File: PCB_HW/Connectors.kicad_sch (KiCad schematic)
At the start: 14 parts, among them J10 Conn_01x04_MountingPin, J11 Conn_01x04_MountingPin, J12 Conn_01x06_MountingPin, J13 Conn_01x08_MountingPin, J14 Conn_01x08, J15 Conn_01x04_MountingPin, J2 Conn_01x04_MountingPin, J3 Conn_01x04_MountingPin, J4 Conn_01x04_MountingPin, J5 Conn_01x04_MountingPin, J6 Conn_01x08_MountingPin, J7 Conn_01x04_MountingPin, J8 Conn_01x06, J9 Conn_01x02_MountingPin

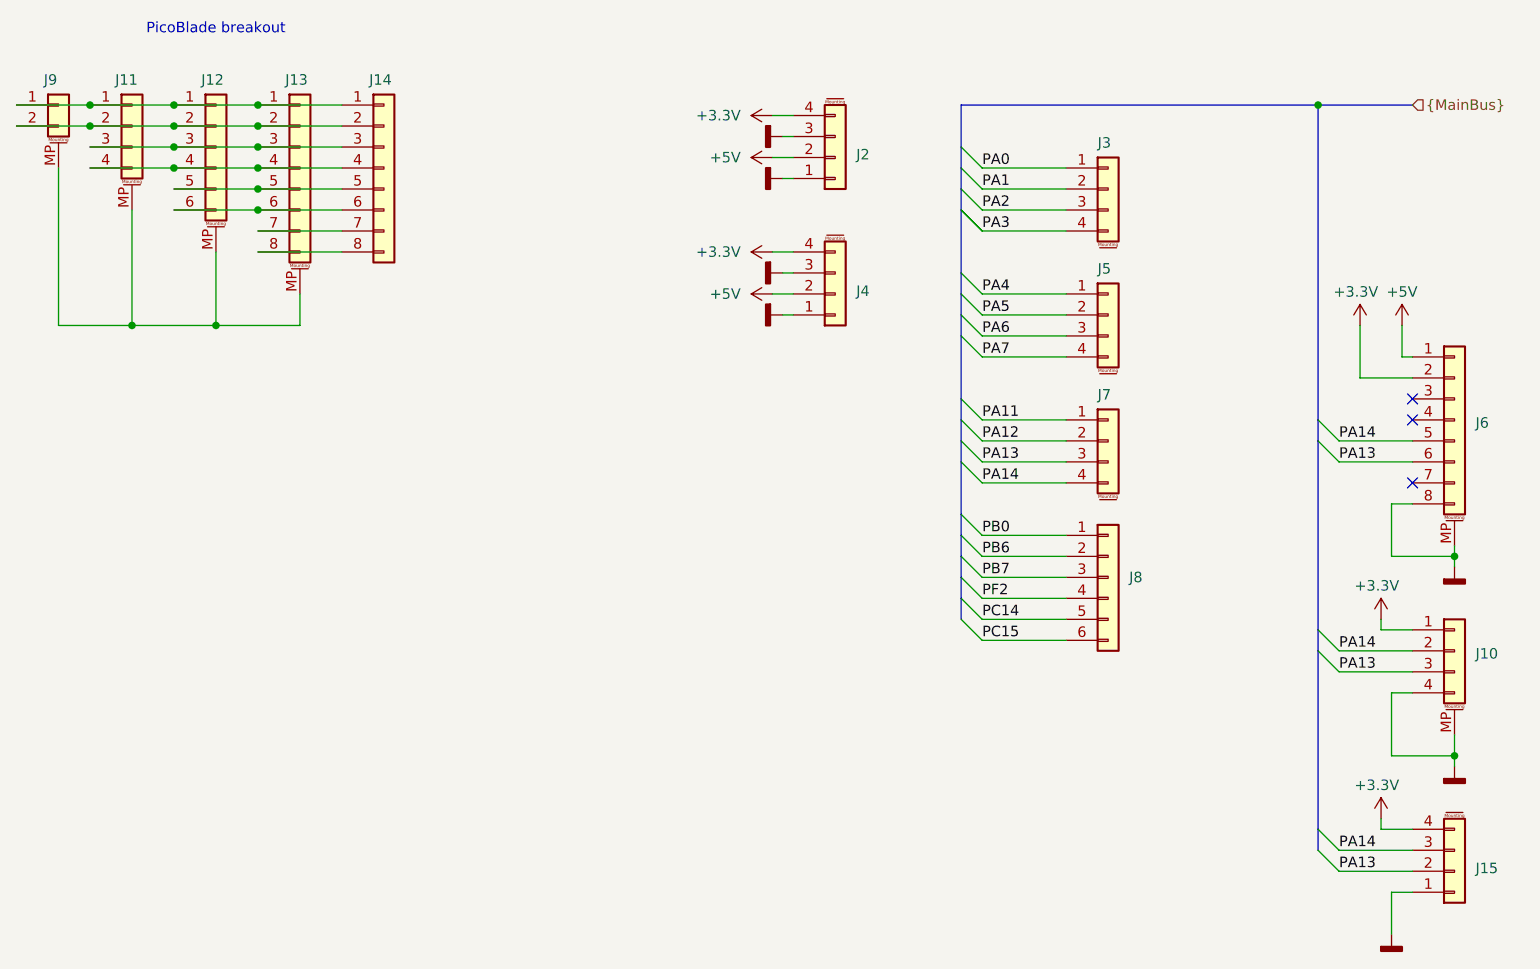
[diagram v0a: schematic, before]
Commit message: Some parts routed
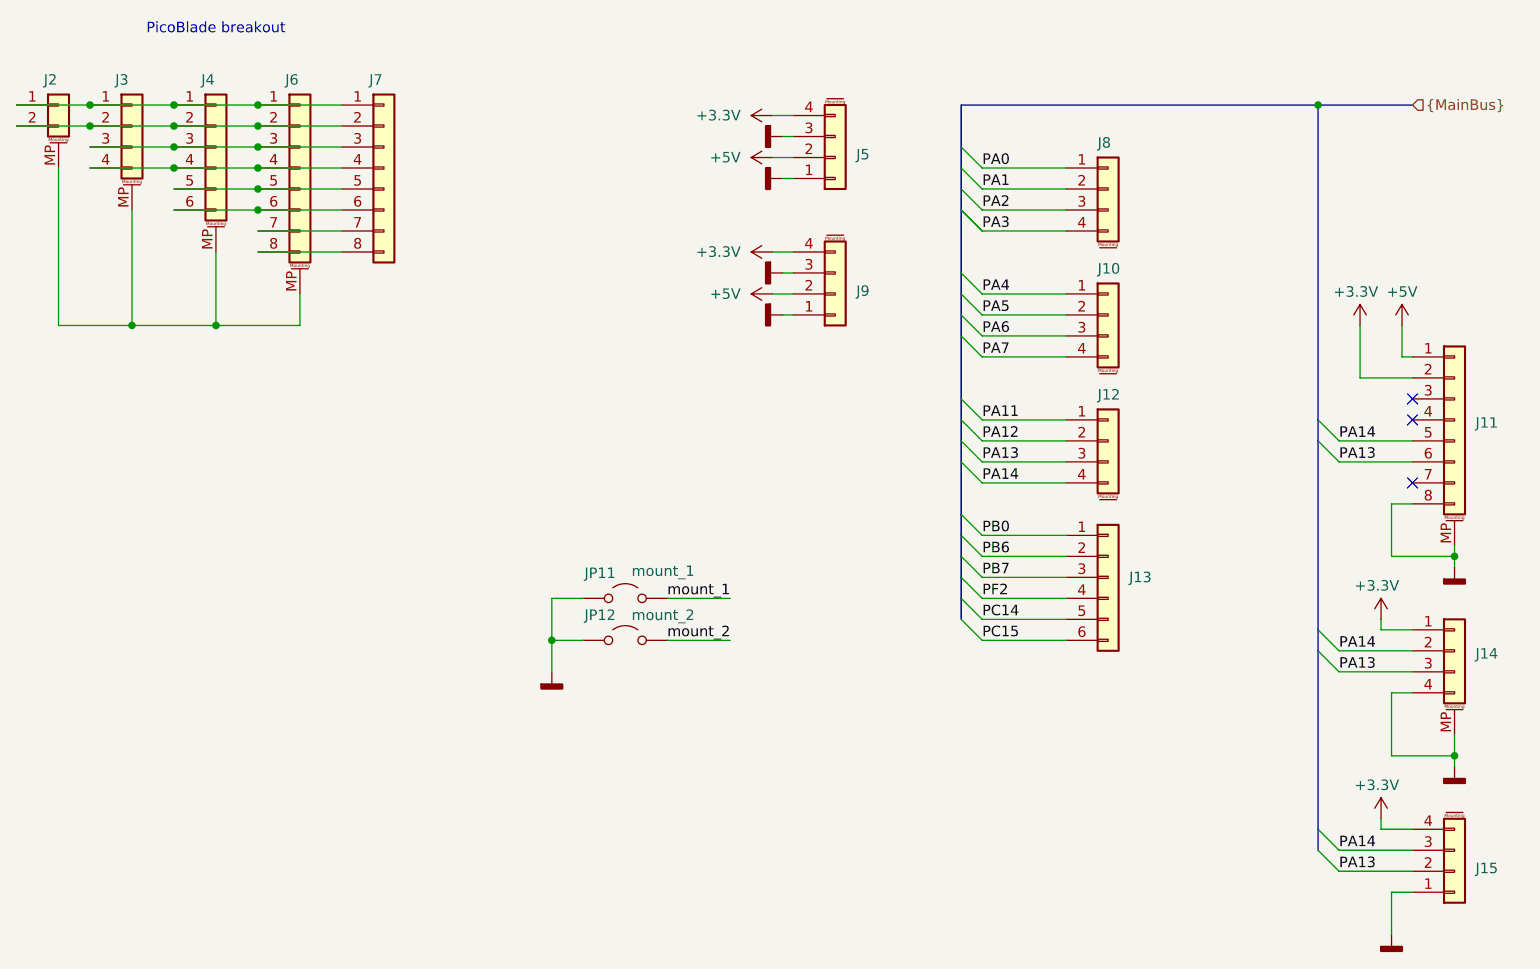
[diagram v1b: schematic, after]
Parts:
- added JP11: mount_1, LocalLib:Jumper_0603, symbol Jumper:Jumper_2_Open
- added JP12: mount_2, LocalLib:Jumper_0603, symbol Jumper:Jumper_2_Open
- J13: renamed from J8; footprint (none) -> Connector_PinHeader_2.54mm:PinHeader_1x06_P2.54mm_Vertical
- J2: renamed from J9; footprint (none) -> Connector_Molex:Molex_PicoBlade_53261-0271_1x02-1MP_P1.25mm_Horizontal
- J3: renamed from J11; footprint (none) -> Connector_Molex:Molex_PicoBlade_53261-0471_1x04-1MP_P1.25mm_Horizontal
- J4: renamed from J12; footprint (none) -> Connector_Molex:Molex_PicoBlade_53261-0671_1x06-1MP_P1.25mm_Horizontal
- J6: renamed from J13; footprint (none) -> Connector_Molex:Molex_PicoBlade_53261-0871_1x08-1MP_P1.25mm_Horizontal
- J7: renamed from J14; footprint (none) -> Connector_PinHeader_2.54mm:PinHeader_1x08_P2.54mm_Vertical
- renumbered J5 to J10, J6 to J11, J7 to J12, J10 to J14, J2 to J5, J3 to J8, J4 to J9
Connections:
- net GNDD: now also JP11.1 (A), JP12.1 (A)
- new net mount_1: JP11.2 (B)
- new net mount_2: JP12.2 (B)
